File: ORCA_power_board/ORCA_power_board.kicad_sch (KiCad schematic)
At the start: 3 parts, among them J17 Vin_motor, J18 data_line_power, J19 +5Vin_cpu

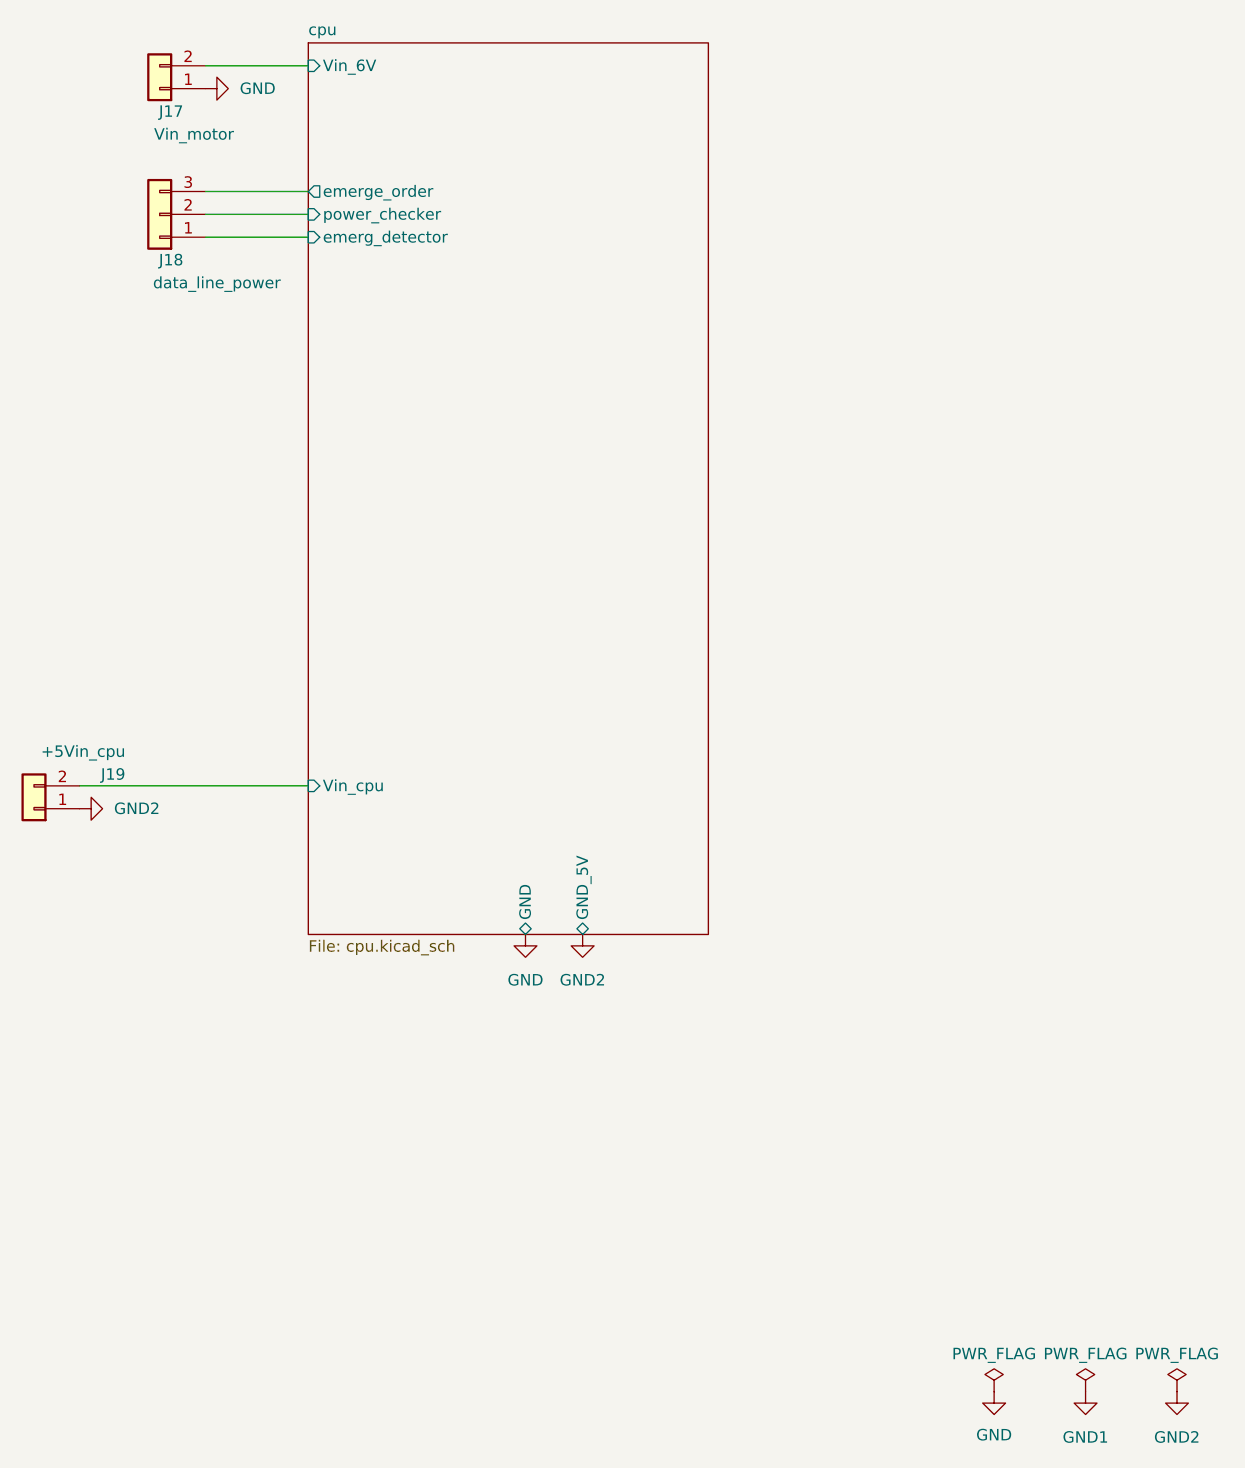
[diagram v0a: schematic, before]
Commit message: change name CORE->power_board moved cput power_borad to CORE
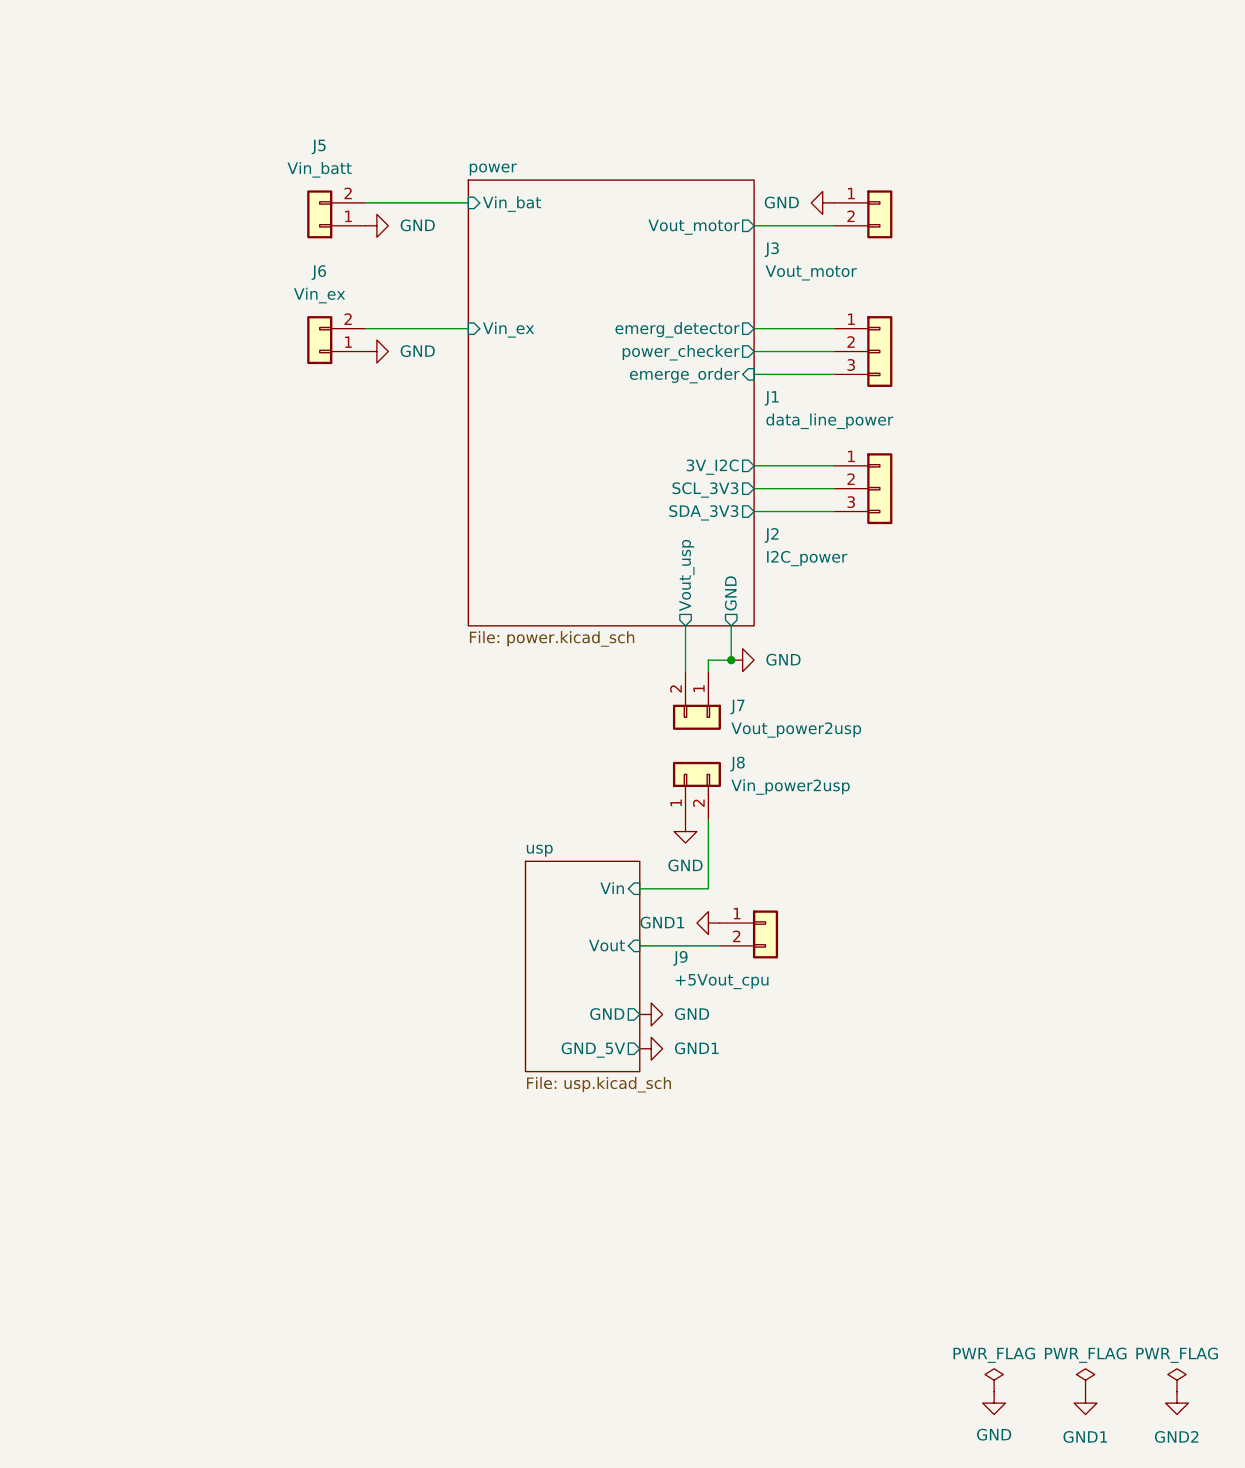
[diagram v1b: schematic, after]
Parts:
- removed J17: Vin_motor, Conn:power_pad, symbol Connector_Generic:Conn_01x02
- removed J18: data_line_power, Connector_JST:JST_XH_B3B-XH-A_1x03_P2.50mm_Vertical, symbol Connector_Generic:Conn_01x03
- removed J19: +5Vin_cpu, Conn:power_pad, symbol Connector_Generic:Conn_01x02
- added J1: data_line_power, Connector_JST:JST_XH_B3B-XH-A_1x03_P2.50mm_Vertical, symbol Connector_Generic:Conn_01x03
- added J2: I2C_power, Connector_JST:JST_XH_B3B-XH-A_1x03_P2.50mm_Vertical, symbol Connector_Generic:Conn_01x03
- added J3: Vout_motor, Conn:power_pad, symbol Connector_Generic:Conn_01x02
- added J5: Vin_batt, Conn:power_pad, symbol Connector_Generic:Conn_01x02
- added J6: Vin_ex, Conn:power_pad, symbol Connector_Generic:Conn_01x02
- added J7: Vout_power2usp, Conn:power_pad, symbol Connector_Generic:Conn_01x02
- added J8: Vin_power2usp, Conn:power_pad, symbol Connector_Generic:Conn_01x02
- added J9: +5Vout_cpu, Conn:power_pad, symbol Connector_Generic:Conn_01x02
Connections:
- net GND: now also J3.1 (Pin_1), J5.1 (Pin_1), J6.1 (Pin_1), J7.1 (Pin_1), J8.1 (Pin_1)
- net GND1: now also J9.1 (Pin_1)
- new net power/3V_I2C: J2.1 (Pin_1)
- new net power/SCL_3V3: J2.2 (Pin_2)
- new net power/SDA_3V3: J2.3 (Pin_3)
- new net power/Vin_bat: J5.2 (Pin_2)
- new net power/Vin_ex: J6.2 (Pin_2)
- new net power/Vout_motor: J3.2 (Pin_2)
- new net power/Vout_usp: J7.2 (Pin_2)
- new net power/emerg_detector: J1.1 (Pin_1)
- new net power/emerge_order: J1.3 (Pin_3)
- new net power/power_checker: J1.2 (Pin_2)
- new net usp/Vin: J8.2 (Pin_2)
- new net usp/Vout: J9.2 (Pin_2)
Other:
- removed sheet cpu
- added sheet power (power.kicad_sch)
- added sheet usp (usp.kicad_sch)

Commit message: complete power_board
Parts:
- J8, J9: footprint Conn:power_pad -> Connector_AMASS:AMASS_XT30U-F_1x02_P5.0mm_Vertical
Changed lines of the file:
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@@
 			)
 		)
-		(property "Footprint" "Conn:power_pad"
+		(property "Footprint" "Connector_AMASS:AMASS_XT30U-F_1x02_P5.0mm_Vertical"
 			(at 158.75 121.92 0)
 			(effects
@@
 			)
 		)
-		(property "Footprint" "Conn:power_pad"
+		(property "Footprint" "Connector_AMASS:AMASS_XT30U-F_1x02_P5.0mm_Vertical"
 			(at 149.86 105.41 0)
 			(effects

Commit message: correct few errors in usp
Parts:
- J8: footprint Connector_AMASS:AMASS_XT30U-F_1x02_P5.0mm_Vertical -> Conn:AMASS_XT30U-F_Vertical_withmodel_female
- J9: footprint Connector_AMASS:AMASS_XT30U-F_1x02_P5.0mm_Vertical -> Conn:AMASS_XT30U-F_Vertical_withmodel_male
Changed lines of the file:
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@@
 (kicad_sch
-	(version 20231120)
+	(version 20250114)
 	(generator "eeschema")
-	(generator_version "8.0")
+	(generator_version "9.0")
 	(paper "A4")
 	(junction
@@
 			)
 		)
-		(property "Footprint" "Connector_AMASS:AMASS_XT30U-F_1x02_P5.0mm_Vertical"
+		(property "Footprint" "Conn:AMASS_XT30U-F_Vertical_withmodel_male"
 			(at 158.75 121.92 0)
 			(effects
@@
 			)
 		)
-		(property "Footprint" "Connector_AMASS:AMASS_XT30U-F_1x02_P5.0mm_Vertical"
+		(property "Footprint" "Conn:AMASS_XT30U-F_Vertical_withmodel_female"
 			(at 149.86 105.41 0)
 			(effects
@@
 		(at 125.73 39.37)
 		(size 31.75 49.53)
+		(exclude_from_sim no)
+		(in_bom yes)
+		(on_board yes)
+		(dnp no)
 		(fields_autoplaced yes)
 		(stroke
@@
 		(at 132.08 115.062)
 		(size 12.7 23.368)
+		(exclude_from_sim no)
+		(in_bom yes)
+		(on_board yes)
+		(dnp no)
 		(fields_autoplaced yes)
 		(stroke
@@
 		)
 	)
+	(embedded_fonts no)
 )
